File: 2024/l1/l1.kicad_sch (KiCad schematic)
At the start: 72 parts, among them J1 Conn_01x04, J2 Conn_01x02, SW1 SW_SPDT, U2 CD74HC4067M, U3 TPS5430DDA, U4 TPS5430DDA

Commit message: final 0.9
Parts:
- added J3: Conn_01x02, Connector_AMASS:AMASS_XT60-M_1x02_P7.20mm_Vertical, symbol Connector_Generic:Conn_01x02
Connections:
- net +12V: now also J3.2 (Pin_2)
- net GND: now also J3.1 (Pin_1)
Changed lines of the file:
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@@
 	(wire
 		(pts
+			(xy 238.76 160.02) (xy 247.65 160.02)
+		)
+		(stroke
+			(width 0)
+			(type default)
+		)
+	)
+	(wire
+		(pts
 			(xy 25.4 41.91) (xy 25.4 36.83)
 		)
@@
 		)
 	)
+	(label "GND"
+		(at 242.57 160.02 180)
+		(fields_autoplaced yes)
+		(effects
+			(font
+				(size 1.27 1.27)
+			)
+			(justify right bottom)
+		)
+	)
 	(label "RXL2"
 		(at 208.28 153.67 0)
@@
 	)
 	(symbol
+		(lib_id "power:+12V")
+		(at 247.65 162.56 90)
+		(unit 1)
+		(exclude_from_sim no)
+		(in_bom yes)
+		(on_board yes)
+		(dnp no)
+		(fields_autoplaced yes)
+		(property "Reference" "#PWR025"
+			(at 251.46 162.56 0)
+			(effects
+				(font
+					(size 1.27 1.27)
+				)
+				(hide yes)
+			)
+		)
+		(property "Value" "+12V"
+			(at 243.84 162.56 90)
+			(effects
+				(font
+					(size 1.27 1.27)
+				)
+				(justify left)
+			)
+		)
+		(property "Footprint" ""
+			(at 247.65 162.56 0)
+			(effects
+				(font
+					(size 1.27 1.27)
+				)
+				(hide yes)
+			)
+		)
+		(property "Datasheet" ""
+			(at 247.65 162.56 0)
+			(effects
+				(font
+					(size 1.27 1.27)
+				)
+				(hide yes)
+			)
+		)
+		(property "Description" ""
+			(at 247.65 162.56 0)
+			(effects
+				(font
+					(size 1.27 1.27)
+				)
+				(hide yes)
+			)
+		)
+		(pin "1"
+		)
+		(instances
+			(project "l1"
+				(path "/d2a4947d-b175-464f-99b5-a0ff44339c9b"
+					(reference "#PWR025")
+					(unit 1)
+				)
+			)
+		)
+	)
+	(symbol
 		(lib_id "power:GND")
 		(at 57.15 185.42 0)
@@
 					(unit 1)
 				)
+			)
+		)
+	)
+	(symbol
+		(lib_id "Connector_Generic:Conn_01x02")
+		(at 252.73 160.02 0)
+		(unit 1)
+		(exclude_from_sim no)
+		(in_bom yes)
+		(on_board yes)
+		(dnp no)
+		(fields_autoplaced yes)
+		(property "Reference" "J3"
+			(at 255.27 160.02 0)
+			(effects
+				(font
+					(size 1.27 1.27)
+				)
+				(justify left)
+			)
+		)
+		(property "Value" "Conn_01x02"
+			(at 255.27 162.56 0)
+			(effects
+				(font
+					(size 1.27 1.27)
+				)
+				(justify left)
+			)
+		)
+		(property "Footprint" "Connector_AMASS:AMASS_XT60-M_1x02_P7.20mm_Vertical"
+			(at 252.73 160.02 0)
+			(effects
+				(font
+					(size 1.27 1.27)
+				)
+				(hide yes)
+			)
+		)
+		(property "Datasheet" "~"
+			(at 252.73 160.02 0)
+			(effects
+				(font
+					(size 1.27 1.27)
+				)
+				(hide yes)
+			)
+		)
+		(property "Description" ""
+			(at 252.73 160.02 0)
+			(effects
+				(font
+					(size 1.27 1.27)
+				)
+				(hide yes)
+			)
+		)
+		(pin "1"
+		)
+		(pin "2"
+		)
+		(instances
+			(project "l1"
+				(path "/d2a4947d-b175-464f-99b5-a0ff44339c9b"
+					(reference "J3")
+					(unit 1)
+				)

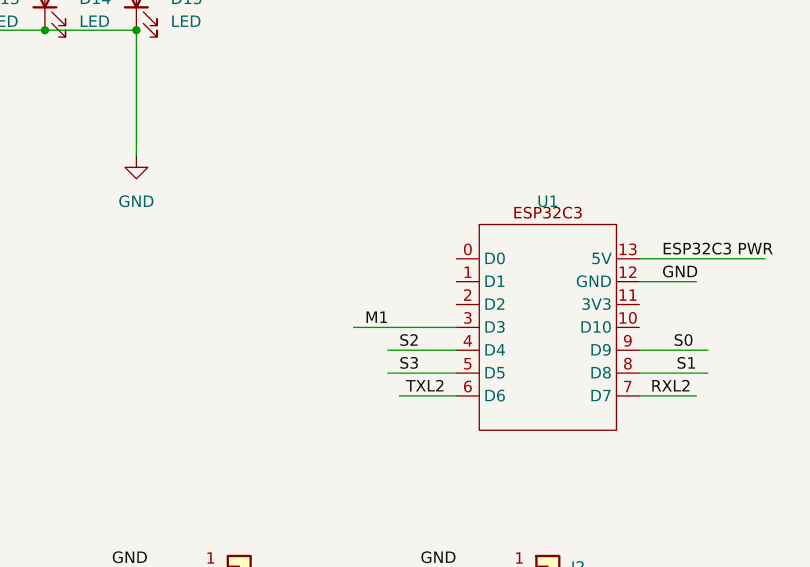
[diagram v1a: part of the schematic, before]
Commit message: final 0.91
fixed:
switched analog signal pin on l1 esp32c3 to a0 since a1 not working
silkscreen is now properly placed
traces are adjusted on l1
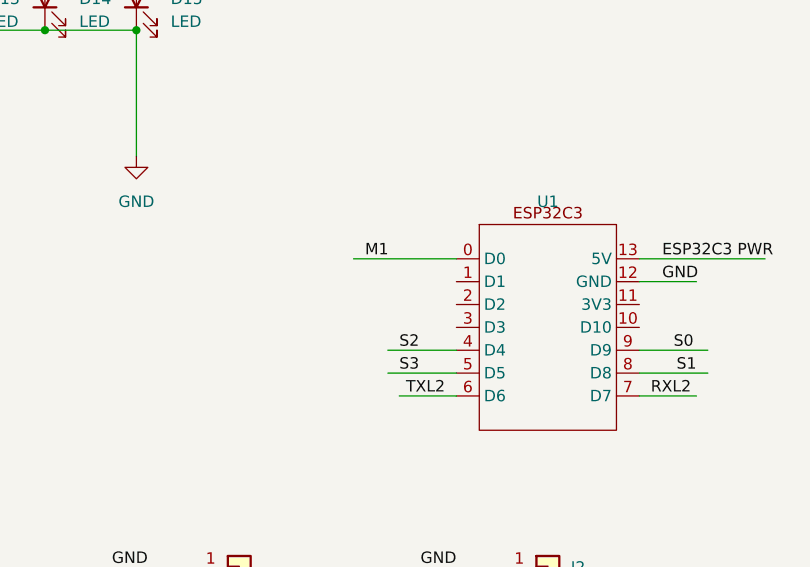
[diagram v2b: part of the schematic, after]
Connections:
- net M1: now also U1.0 (D0); no longer U1.3 (D3)
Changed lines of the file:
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@@
-	(wire
-		(pts
-			(xy 231.14 124.46) (xy 242.57 124.46)
-		)
-		(stroke
-			(width 0)
-			(type default)
-		)
-	)
 	(wire
 		(pts
@@
 	(wire
 		(pts
+			(xy 231.14 116.84) (xy 242.57 116.84)
+		)
+		(stroke
+			(width 0)
+			(type default)
+		)
+	)
+	(wire
+		(pts
 			(xy 102.87 36.83) (xy 115.57 36.83)
 		)
@@
 	)
 	(label "M1"
-		(at 232.41 124.46 0)
+		(at 232.41 116.84 0)
 		(fields_autoplaced yes)
 		(effects
